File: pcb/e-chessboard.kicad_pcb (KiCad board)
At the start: 4 copper layers, 170 x 170 mm, 66 parts, among them J1 POWER, J2 UART, Q1 BC847, Q2 BC847, SW1 Reset, SW2 Boot, U1 ESP32-WROOM-32U, U10 MAGNET_LDR, U11 MAGNET_LDR, U12 MAGNET_LDR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

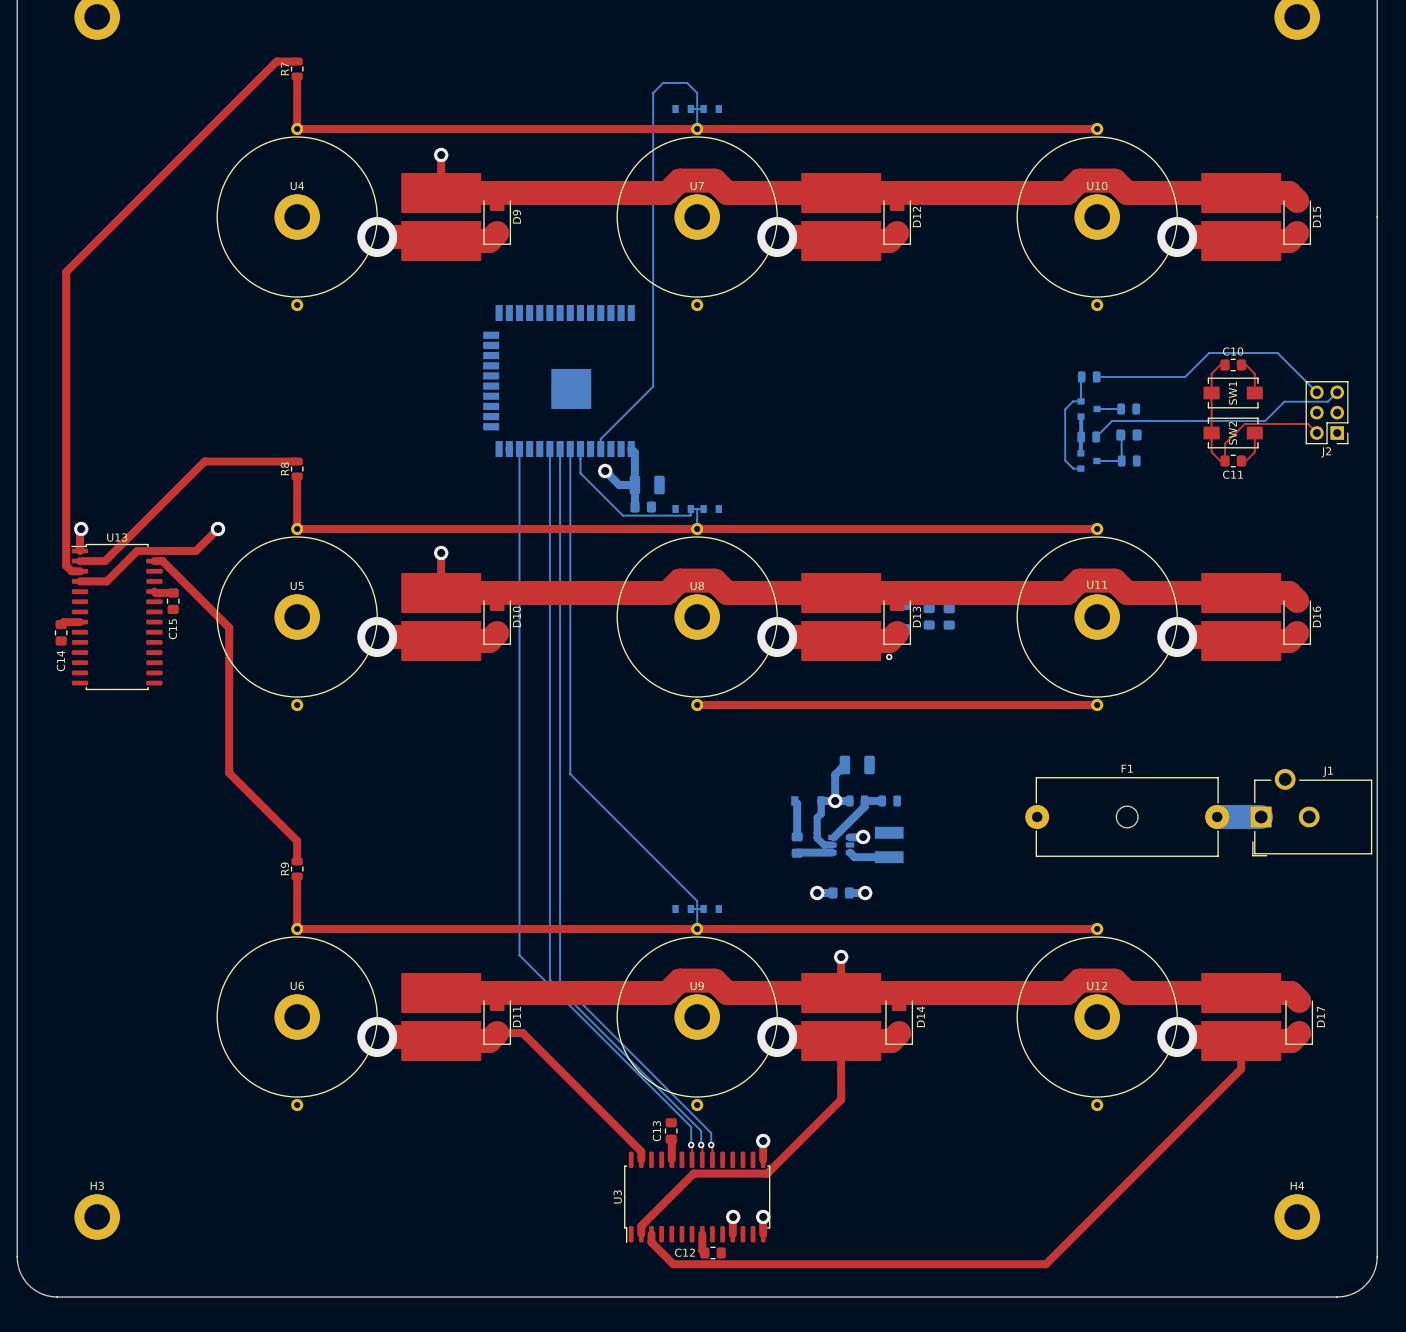
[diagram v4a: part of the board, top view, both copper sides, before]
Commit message: fix(kicad): laying all spi traces
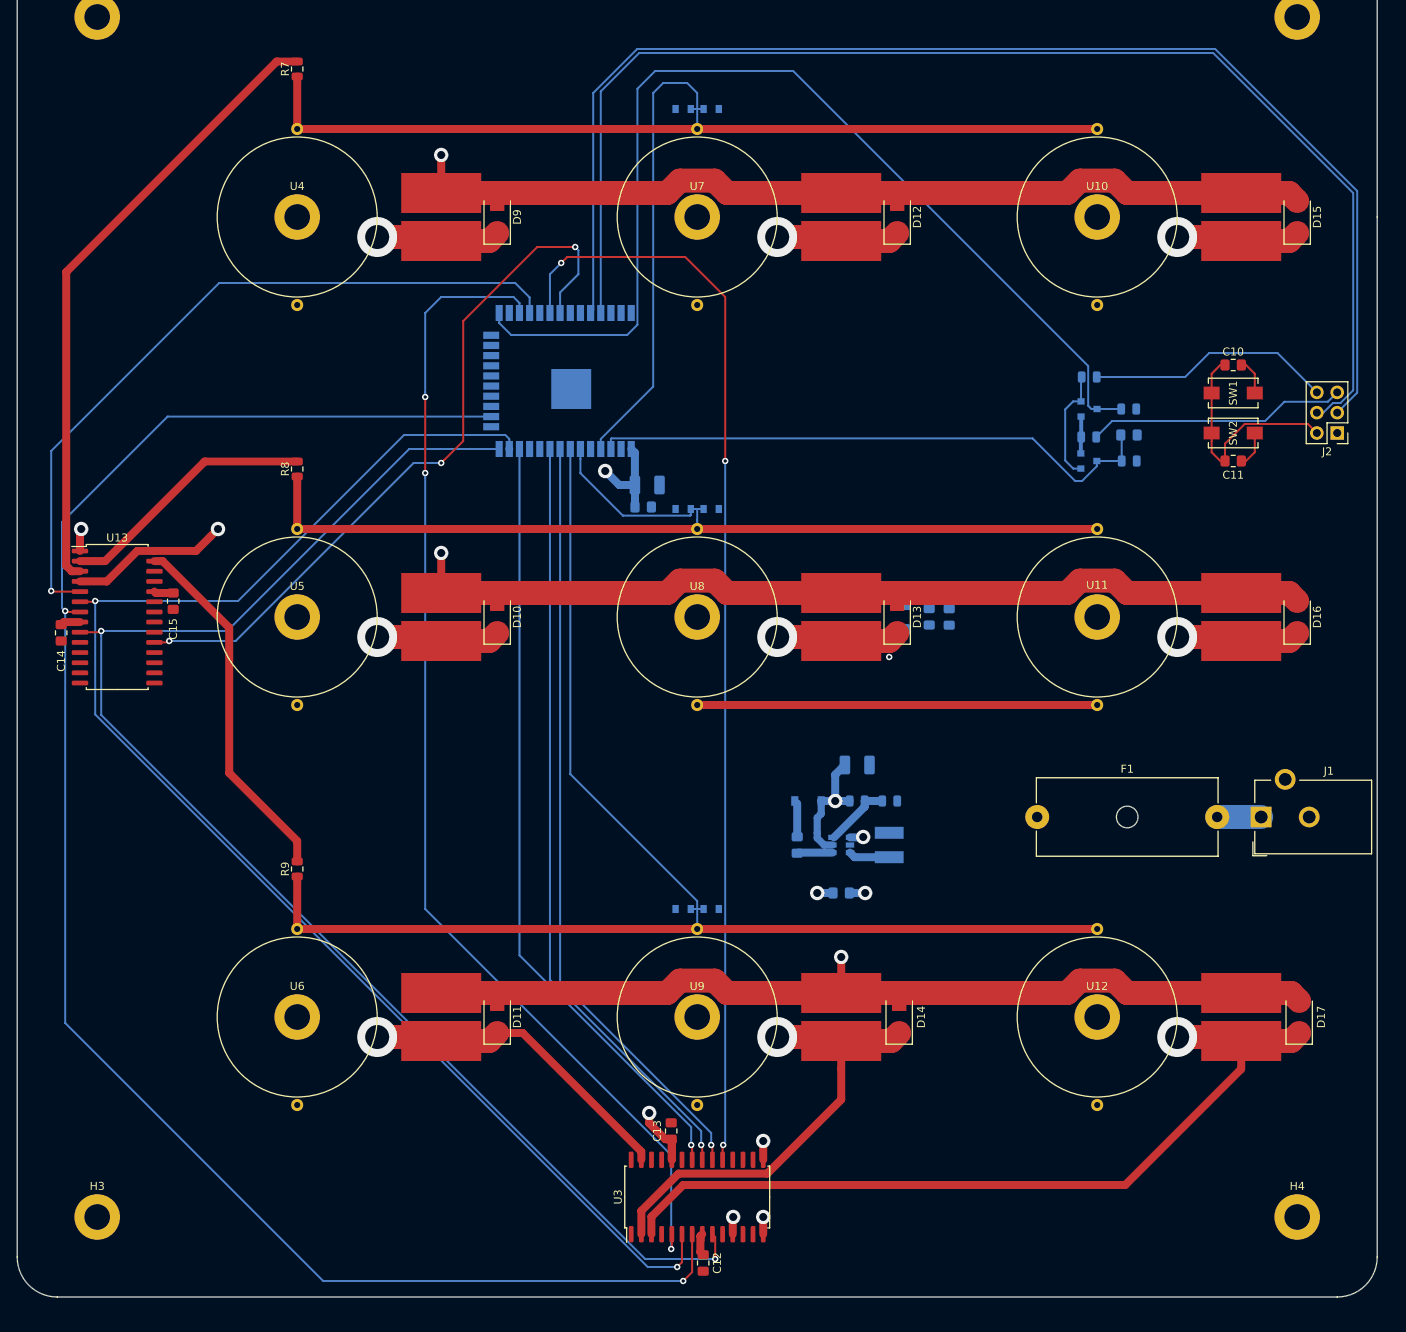
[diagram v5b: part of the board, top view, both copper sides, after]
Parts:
- moved C12 1.75 mm to (135.8, 215.8), turned to 90 degrees
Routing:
- net MOSI: track 0.00 -> 220.7 mm, vias 0 -> 2
- net SCLK: track 0.02 -> 183.7 mm, vias 0 -> 2
- net MISO: track 0.00 -> 180.5 mm, vias 0 -> 2
- net UART_RX: track 0.00 -> 161.5 mm
- net UART_TX: track 0.00 -> 161.3 mm
- net MAG_CS: track 0.00 -> 145.8 mm, vias 0 -> 3
- net MAG_EN: track 0.00 -> 137.7 mm, vias 0 -> 3
- net IO0: track 7.55 -> 135.5 mm
- net LDR_CS: track 0.00 -> 92.3 mm, vias 0 -> 1
- net LDR_EN: track 0.00 -> 91.2 mm, vias 0 -> 3
- net EN: track 10.9 -> 76.6 mm
- net +12V: track 31.3 -> 38.7 mm, vias 4 -> 5
- net MAG_COL_1: track 236.6 -> 234.2 mm
- net MAG_COL_2: track 187.0 -> 188.1 mm

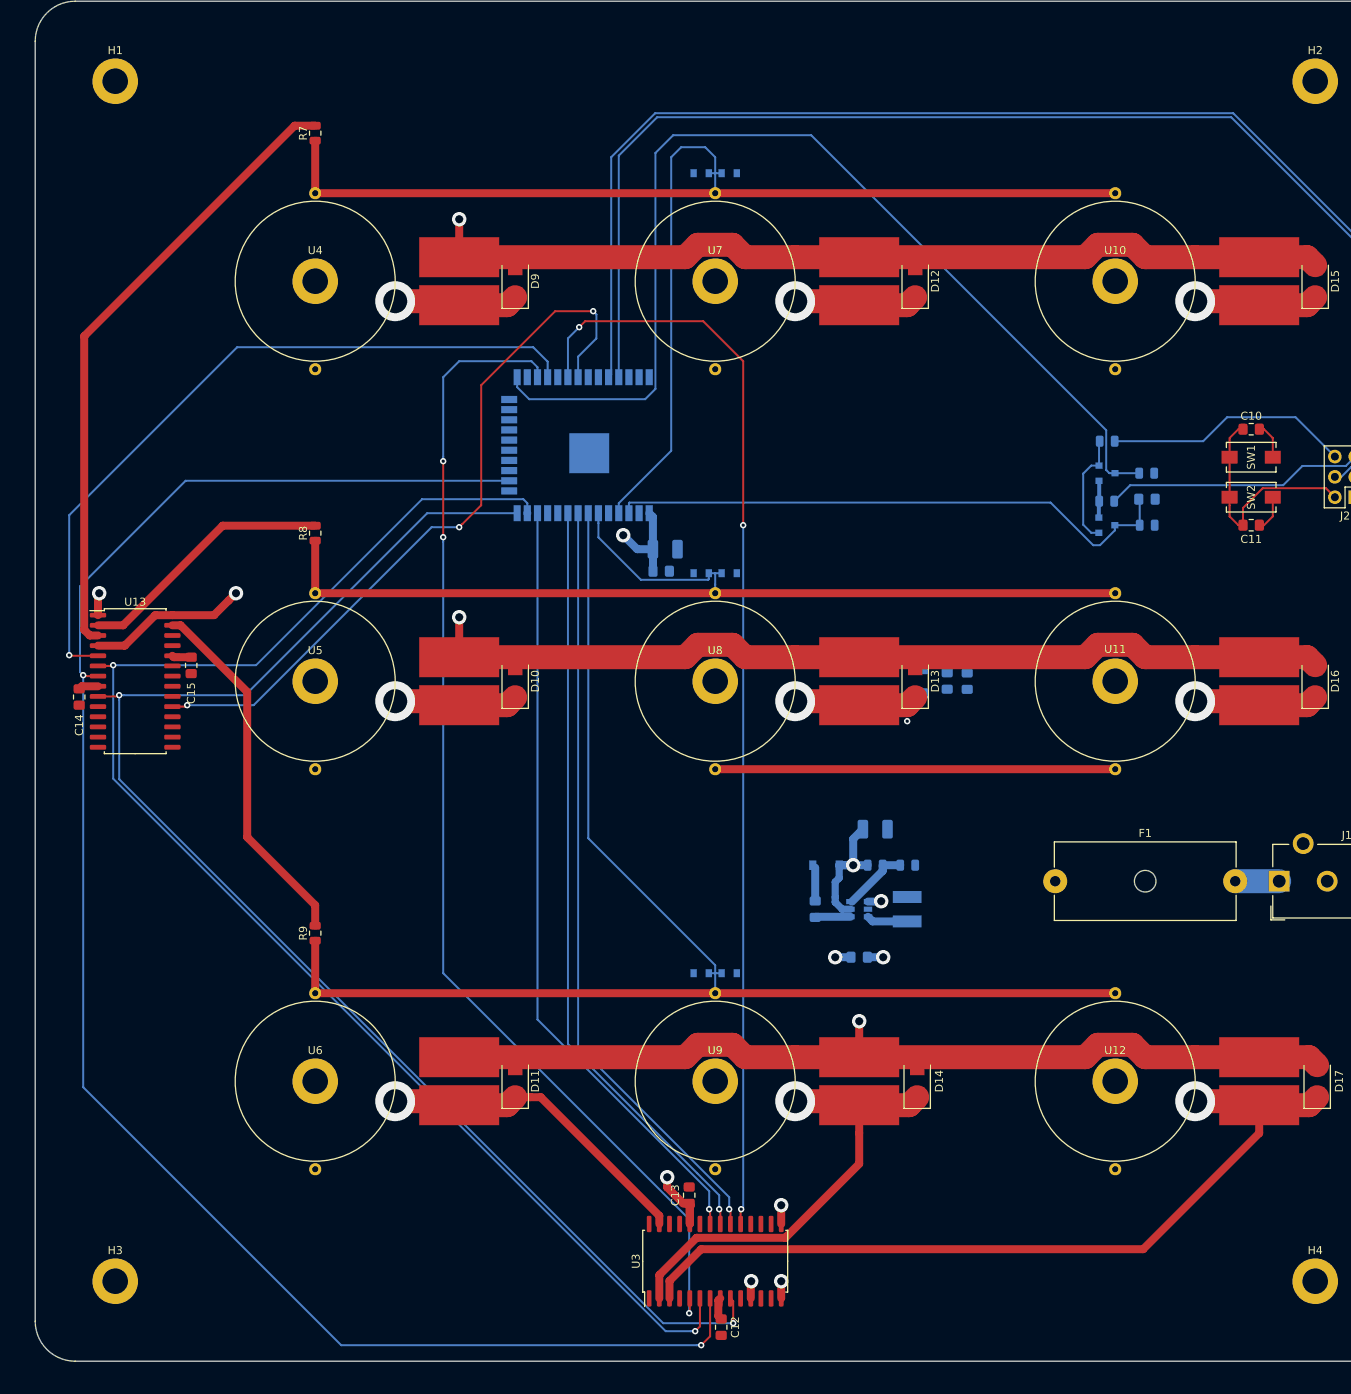
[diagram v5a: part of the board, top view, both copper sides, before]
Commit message: fix(kicad): fixing all erc error and warnings
Ready for first release!!!
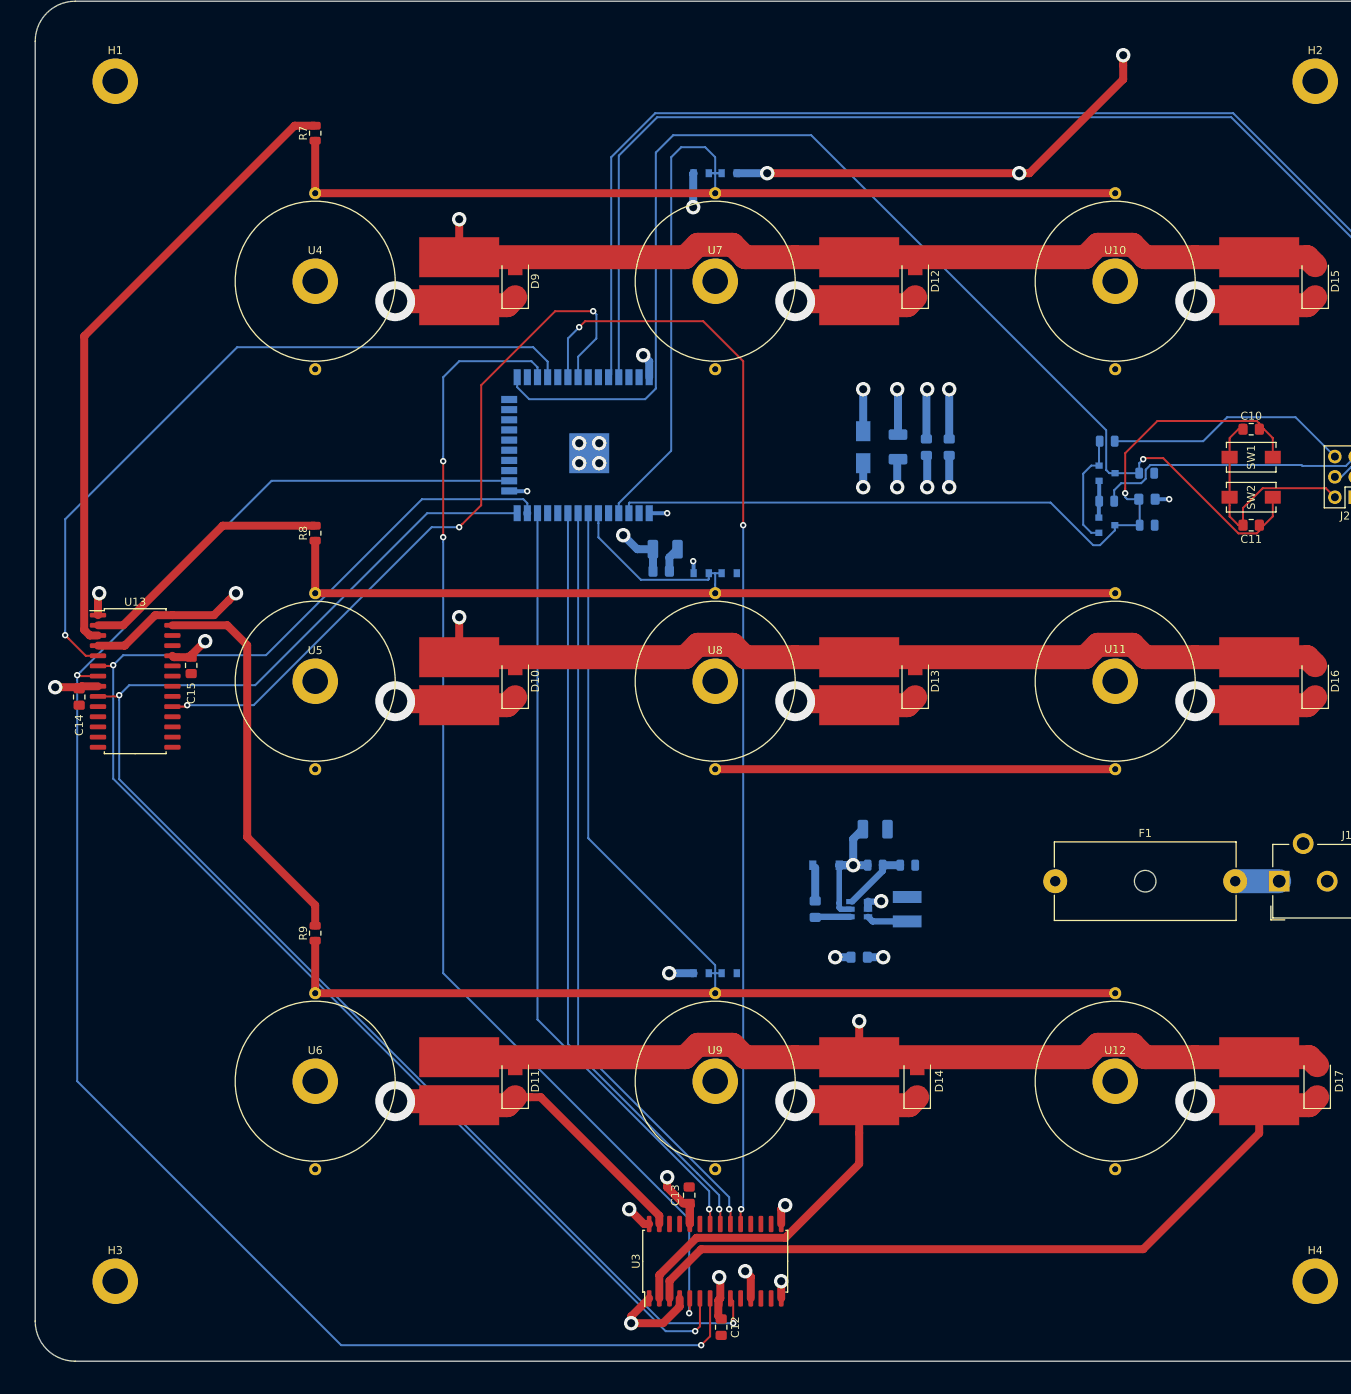
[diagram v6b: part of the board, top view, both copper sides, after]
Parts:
- moved C1 29.4 mm to (157.8, 105.7)
- moved D3 29.4 mm to (153.5, 105.8)
- moved C2 29.3 mm to (161.4, 105.8)
- moved C5 29.3 mm to (164.2, 105.8)
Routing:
- net +3V3: track 5.30 -> 70.4 mm, vias 0 -> 5
- net +12V: track 38.7 -> 80.9 mm, vias 5 -> 12
- net MAG_ROW_3: track 171.9 -> 144.1 mm
- net GND: track 110.7 -> 138.4 mm, vias 3 -> 18
- net EN: track 76.6 -> 103.2 mm, vias 0 -> 1
- net IO0: track 135.5 -> 156.8 mm, vias 0 -> 1
- net MOSI: track 220.7 -> 215.4 mm
- net LDR_ROW3: track 45.5 -> 49.0 mm
- net RTS: track 32.4 -> 34.2 mm
- net LDR_ADC1: track 166.4 -> 168.0 mm
- net MAG_ROW_2: track 233.1 -> 231.9 mm
- net MAG_ROW_1: track 327.7 -> 326.7 mm
- net LDR_CS: track 92.3 -> 91.6 mm
- net MAG_COL_2: vias 4 -> 3
